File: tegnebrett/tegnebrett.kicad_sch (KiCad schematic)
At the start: 45 parts, among them J1 FH12-45S-0.5SH55, J2 FH12-6S-1SH55, J3 Conn_ST_STDC14, J4 USB-A1HSW6, J5 MCU_Header_Pin, SW1 SW_Push, SW2 SW_Push, SW3 MCU_Button, SW4 Reset, SW5 Undo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

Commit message: fix: fix footprint paths for symbols
After moving the footprints around, some symbols were without
footprints.
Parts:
- J4: footprint USB-A1HSW6:OST_USB-A1HSW6 -> tegnebrett_modules:OST_USB-A1HSW6
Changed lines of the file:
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@@
 			)
 		)
-		(property "Footprint" "USB-A1HSW6:OST_USB-A1HSW6"
+		(property "Footprint" "tegnebrett_modules:OST_USB-A1HSW6"
 			(at 254 73.66 0)
 			(effects

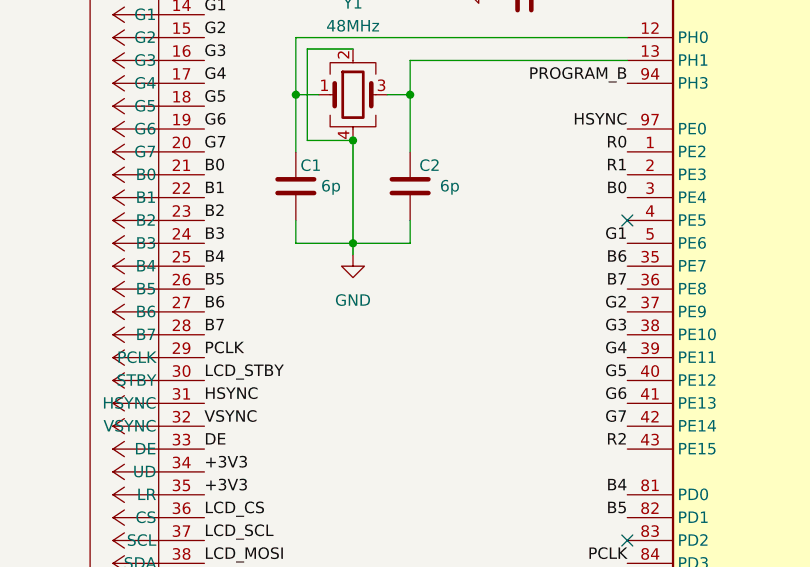
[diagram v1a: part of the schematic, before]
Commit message: fix: Fix error saying that Ground pin isn't powered by power source.
Did this by adding a PWR_FLAG to the schematic.
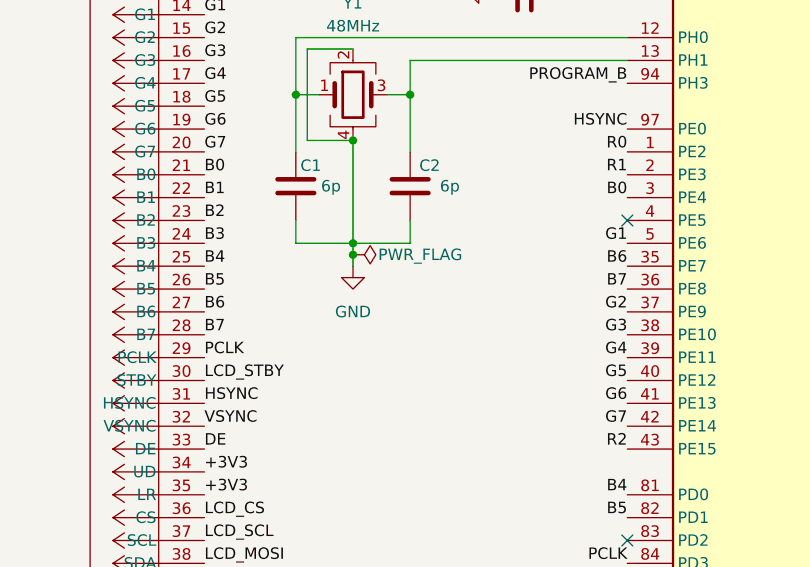
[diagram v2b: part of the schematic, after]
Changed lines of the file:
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@@
 	)
 	(junction
+		(at 53.34 90.17)
+		(diameter 0)
+		(color 0 0 0 0)
+	)
+	(junction
 		(at 231.14 30.48)
 		(diameter 0)
@@
 	(wire
 		(pts
+			(xy 53.34 90.17) (xy 53.34 91.44)
+		)
+		(stroke
+			(width 0)
+			(type default)
+		)
+	)
+	(wire
+		(pts
 			(xy 60.96 156.21) (xy 60.96 168.91)
 		)
@@
 	)
 	(symbol
+		(lib_id "power:PWR_FLAG")
+		(at 53.34 90.17 270)
+		(unit 1)
+		(exclude_from_sim no)
+		(in_bom yes)
+		(on_board yes)
+		(dnp no)
+		(property "Reference" "#FLG08"
+			(at 55.245 90.17 0)
+			(effects
+				(font
+					(size 1.27 1.27)
+				)
+				(hide yes)
+			)
+		)
+		(property "Value" "PWR_FLAG"
+			(at 56.134 90.17 90)
+			(effects
+				(font
+					(size 1.27 1.27)
+				)
+				(justify left)
+			)
+		)
+		(property "Footprint" ""
+			(at 53.34 90.17 0)
+			(effects
+				(font
+					(size 1.27 1.27)
+				)
+				(hide yes)
+			)
+		)
+		(property "Datasheet" "~"
+			(at 53.34 90.17 0)
+			(effects
+				(font
+					(size 1.27 1.27)
+				)
+				(hide yes)
+			)
+		)
+		(property "Description" "Special symbol for telling ERC where power comes from"
+			(at 53.34 90.17 0)
+			(effects
+				(font
+					(size 1.27 1.27)
+				)
+				(hide yes)
+			)
+		)
+		(pin "1"
+		)
+		(instances
+			(project ""
+				(path "/d9a31669-c5f1-42a7-9461-3df04b9a4e62"
+					(reference "#FLG08")
+					(unit 1)
+				)
+			)
+		)
+	)
+	(symbol
 		(lib_id "power:GND")
 		(at 162.56 96.52 90)
@@
 	(symbol
 		(lib_id "power:GND")
-		(at 53.34 90.17 0)
+		(at 53.34 91.44 0)
 		(unit 1)
 		(exclude_from_sim no)
@@
 		(fields_autoplaced yes)
 		(property "Reference" "#PWR01"
-			(at 53.34 96.52 0)
+			(at 53.34 97.79 0)
 			(effects
 				(font
@@
 		)
 		(property "Value" "GND"
-			(at 53.34 95.25 0)
+			(at 53.34 96.52 0)
 			(effects
 				(font
@@
 		)
 		(property "Footprint" ""
-			(at 53.34 90.17 0)
+			(at 53.34 91.44 0)
 			(effects
 				(font
@@
 		)
 		(property "Datasheet" ""
-			(at 53.34 90.17 0)
+			(at 53.34 91.44 0)
 			(effects
 				(font
@@
 		)
 		(property "Description" "Power symbol creates a global label with name \"GND\" , ground"
-			(at 53.34 90.17 0)
+			(at 53.34 91.44 0)
 			(effects
 				(font

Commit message: feat: add FH12 symbols
These were lost somewhere in the process. We're getting KiCAD warnings
because the former library no longer exists.
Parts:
- J1: symbol 2025-09-15_10-55-53:FH12-45S-0.5SH55 -> tegnebrett_symbols:FH12-45S-0.5SH55
- J2: symbol 2025-09-15_09-29-33:FH12-6S-1SH55 -> tegnebrett_symbols:FH12-6S-1SH55
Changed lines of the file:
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@@
 	)
 	(symbol
-		(lib_id "2025-09-15_09-29-33:FH12-6S-1SH55")
+		(lib_id "tegnebrett_symbols:FH12-6S-1SH55")
 		(at 36.83 166.37 180)
 		(unit 1)
@@
 		)
 		(property "Footprint" "tegnebrett_modules:CON6_1X6_DRBF_HST_HIR"
-			(at 36.83 166.37 0)
+			(at 32.512 175.26 0)
 			(effects
 				(font
@@
 		)
 		(property "Datasheet" "FH12-6S-1SH55"
-			(at 36.83 166.37 0)
+			(at 32.258 177.292 0)
 			(effects
 				(font
@@
 		)
 		(property "Sim.Library" "./"
-			(at 36.83 166.37 0)
+			(at 36.83 170.688 0)
 			(effects
 				(font
@@
 		)
 		(property "Sim.Name" "<unbekannt>"
-			(at 36.83 166.37 0)
+			(at 39.37 173.228 0)
 			(effects
 				(font
@@
 	)
 	(symbol
-		(lib_id "2025-09-15_10-55-53:FH12-45S-0.5SH55")
+		(lib_id "tegnebrett_symbols:FH12-45S-0.5SH55")
 		(at 36.83 30.48 0)
 		(mirror y)

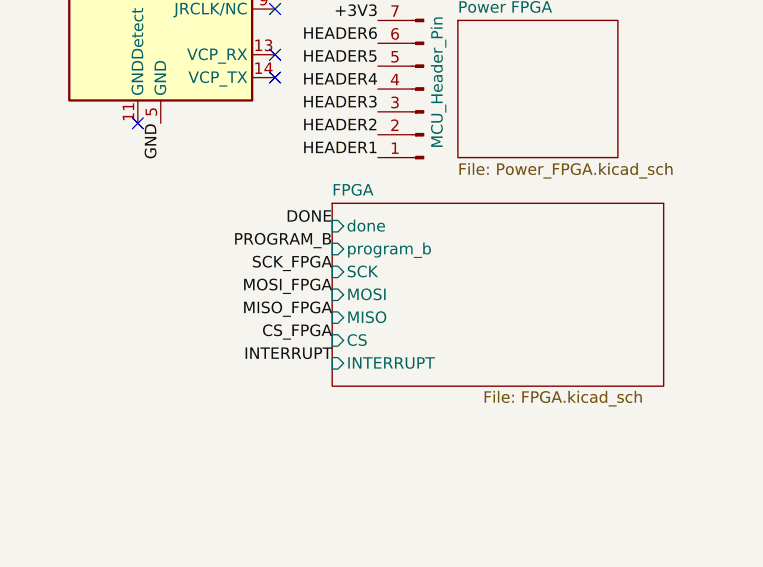
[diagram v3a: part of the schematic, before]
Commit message: refactor: Update label names for hierarchical labels.
Renamed the hierarchical labels in FPGA.kicad_sch, they now are named
the say as the local labels in tegnebrett.kicad_sch

This results in KiCAD no longer throwing any warnings telling us that we
have labels which only differ in casing (upper case / lower case).
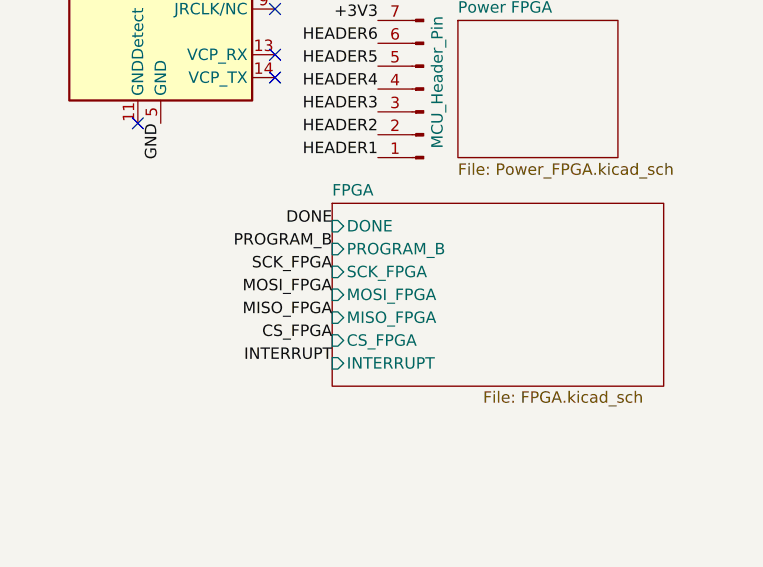
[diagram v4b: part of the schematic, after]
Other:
- sheet FPGA ports: added CS_FPGA, DONE, MISO_FPGA, MOSI_FPGA, PROGRAM_B, SCK_FPGA; removed CS, MISO, MOSI, SCK, done, program_b
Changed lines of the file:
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@@
 	)
 	(label "DONE"
-		(at 246.38 132.08 180)
-		(effects
-			(font
-				(size 1.27 1.27)
-			)
-			(justify right bottom)
-		)
-	)
-	(label "DONE"
 		(at 144.78 109.22 0)
 		(effects
@@
 		)
 	)
+	(label "DONE"
+		(at 246.38 132.08 180)
+		(effects
+			(font
+				(size 1.27 1.27)
+			)
+			(justify right bottom)
+		)
+	)
 	(label "INTERRUPT"
 		(at 246.38 147.32 180)
@@
 			)
 		)
-		(pin "done" input
+		(pin "DONE" input
 			(at 246.38 132.08 180)
 			(effects
@@
 			)
 		)
-		(pin "program_b" input
+		(pin "PROGRAM_B" input
 			(at 246.38 134.62 180)
 			(effects
@@
 			)
 		)
-		(pin "CS" input
+		(pin "CS_FPGA" input
 			(at 246.38 144.78 180)
 			(effects
@@
 			)
 		)
-		(pin "MISO" input
+		(pin "MISO_FPGA" input
 			(at 246.38 142.24 180)
 			(effects
@@
 			)
 		)
-		(pin "MOSI" input
+		(pin "MOSI_FPGA" input
 			(at 246.38 139.7 180)
 			(effects
@@
 			)
 		)
-		(pin "SCK" input
+		(pin "SCK_FPGA" input
 			(at 246.38 137.16 180)
 			(effects

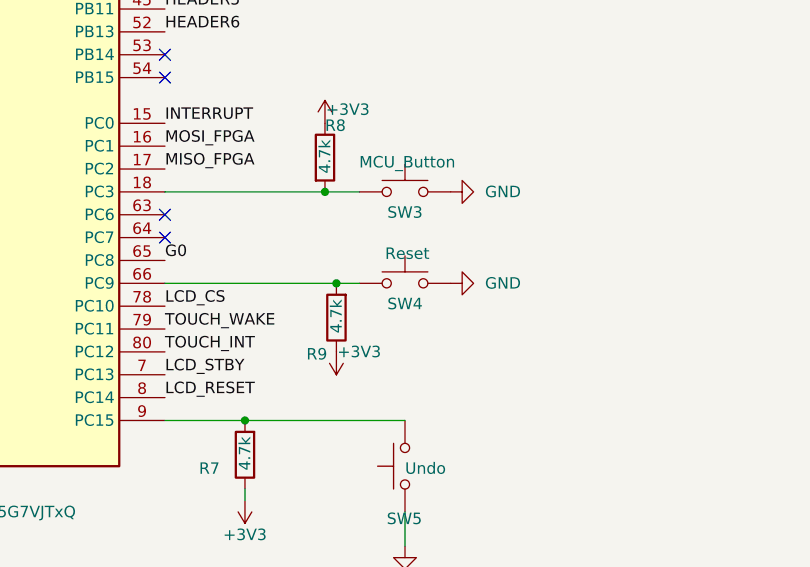
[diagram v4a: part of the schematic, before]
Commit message: fix: add separate symbols for larger switches.
They need pin1 and pin3, not pin1 and pin2.
The PCB editor throws an error when pin3 is not present on the button
symbol.
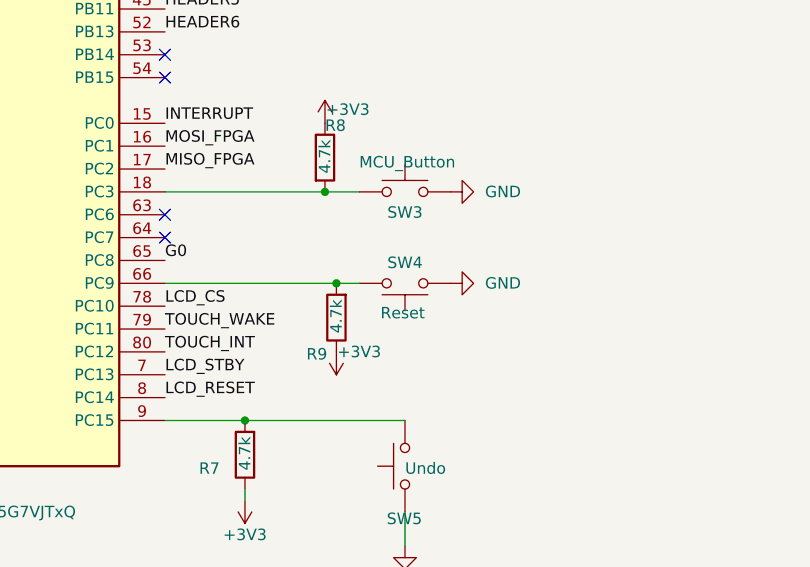
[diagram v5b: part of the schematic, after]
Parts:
- SW4, SW5: symbol Switch:SW_Push -> tegnebrett_symbols:SW_Push_1_3
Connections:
- net GND: now also SW4.1; no longer SW4.2
- net at R9.2, U1.66 (PC9): now also SW4.3; no longer SW4.1
- net at R7.2, U1.9 (PC15): now also SW5.3; no longer SW5.2
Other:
- moved on the sheet: SW4
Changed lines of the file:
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@@
 	)
 	(symbol
-		(lib_id "Switch:SW_Push")
-		(at 171.45 154.94 0)
+		(lib_id "tegnebrett_symbols:SW_Push_1_3")
+		(at 171.45 154.94 180)
 		(unit 1)
 		(exclude_from_sim no)
@@
 		(dnp no)
 		(property "Reference" "SW4"
-			(at 171.45 157.226 0)
+			(at 171.45 152.654 0)
 			(effects
 				(font
@@
 		)
 		(property "Value" "Reset"
-			(at 171.704 151.638 0)
+			(at 171.196 158.242 0)
 			(effects
 				(font
@@
 		)
 		(property "Footprint" "tegnebrett_modules:SW_KS11R23CQD"
-			(at 171.45 149.86 0)
+			(at 171.45 160.02 0)
 			(effects
 				(font
@@
 		)
 		(property "Datasheet" "~"
-			(at 171.45 149.86 0)
+			(at 171.45 160.02 0)
 			(effects
 				(font
@@
 		)
 		(property "Description" "Push button switch, generic, two pins"
-			(at 171.45 154.94 0)
-			(effects
-				(font
-					(size 1.27 1.27)
-				)
-				(hide yes)
-			)
-		)
-		(pin "1"
-		)
-		(pin "2"
+			(at 171.45 150.368 0)
+			(effects
+				(font
+					(size 1.27 1.27)
+				)
+				(hide yes)
+			)
+		)
+		(pin "1"
+		)
+		(pin "3"
 		)
 		(instances
@@
 	)
 	(symbol
-		(lib_id "Switch:SW_Push")
+		(lib_id "tegnebrett_symbols:SW_Push_1_3")
 		(at 171.45 175.26 90)
 		(unit 1)
@@
 		)
 		(property "Description" "Push button switch, generic, two pins"
-			(at 171.45 175.26 0)
-			(effects
-				(font
-					(size 1.27 1.27)
-				)
-				(hide yes)
-			)
-		)
-		(pin "1"
-		)
-		(pin "2"
-		)
-		(instances
+			(at 176.022 175.26 0)
+			(effects
+				(font
+					(size 1.27 1.27)
+				)
+				(hide yes)
+			)
+		)
+		(pin "1"
+		)
+		(pin "3"
+		)
+		(instances

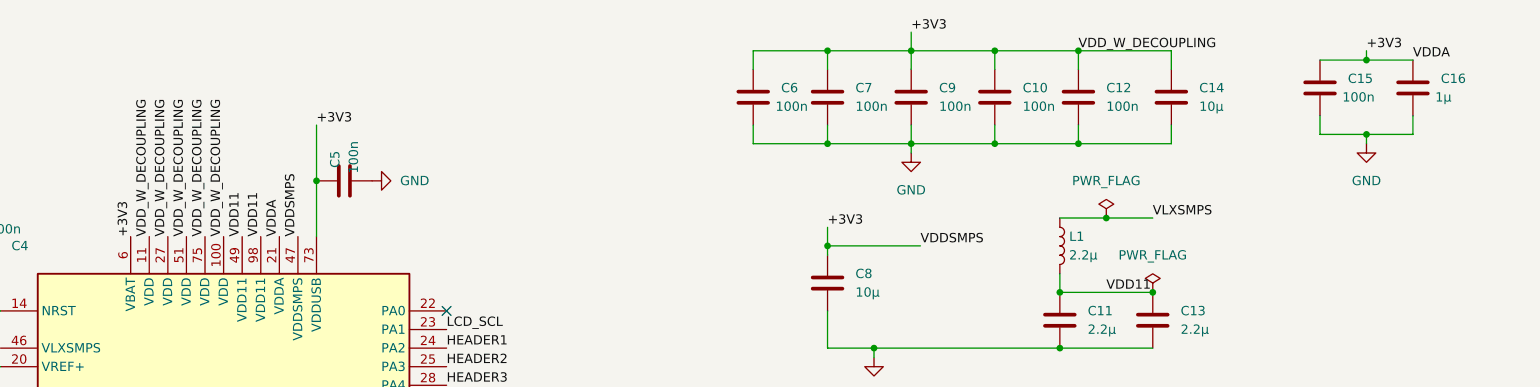
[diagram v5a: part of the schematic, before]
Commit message: fix: remove unused net labels in main MCU sheet
I had used labels called *VDD_W_DECOUPLING* and so forth, but these were
identical in nature to +3V3. The chatbot is saying that we ideally
should have different subnets (whatever that means). Would be necessary
in larger projects, but it's fine to have just +3V3 in this small
schematic/PCB layout.

This removed the last warning in the ERC checker for the schematic.
We're now at 0 errors and 0 warnings there.
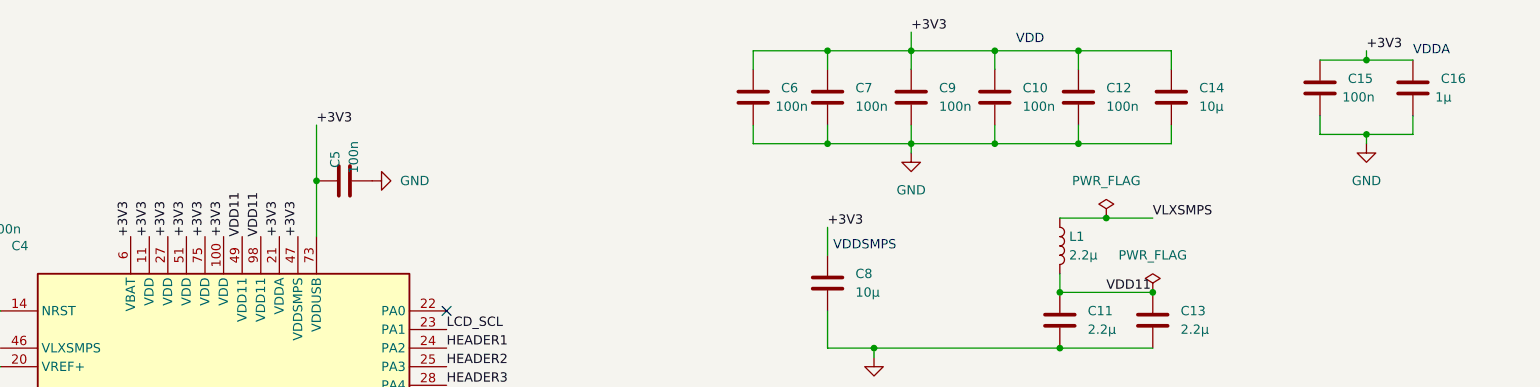
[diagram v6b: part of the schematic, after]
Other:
- note added: "VDD"
- note added: "VDDA"
- note added: "VDDSMPS"
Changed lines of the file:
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@@
 	(generator_version "9.0")
 	(paper "A4")
+	(text "VDD"
+		(exclude_from_sim no)
+		(at 224.536 16.256 0)
+		(effects
+			(font
+				(size 1.27 1.27)
+			)
+		)
+	)
+	(text "VDDSMPS"
+		(exclude_from_sim no)
+		(at 201.93 44.45 0)
+		(effects
+			(font
+				(size 1.27 1.27)
+			)
+		)
+	)
+	(text "VDDA"
+		(exclude_from_sim no)
+		(at 279.4 17.78 0)
+		(effects
+			(font
+				(size 1.27 1.27)
+			)
+		)
+	)
 	(junction
 		(at 228.6 50.8)
@@
 	(junction
 		(at 231.14 30.48)
-		(diameter 0)
-		(color 0 0 0 0)
-	)
-	(junction
-		(at 196.85 44.45)
 		(diameter 0)
 		(color 0 0 0 0)
@@
 	(wire
 		(pts
-			(xy 196.85 41.91) (xy 196.85 44.45)
-		)
-		(stroke
-			(width 0)
-			(type default)
-		)
-	)
-	(wire
-		(pts
 			(xy 240.03 76.2) (xy 243.84 76.2)
 		)
@@
 	(wire
 		(pts
-			(xy 196.85 44.45) (xy 209.55 44.45)
-		)
-		(stroke
-			(width 0)
-			(type default)
-		)
-	)
-	(wire
-		(pts
 			(xy 54.61 158.75) (xy 66.04 158.75)
 		)
@@
 	(wire
 		(pts
-			(xy 196.85 44.45) (xy 196.85 45.72)
+			(xy 196.85 41.91) (xy 196.85 45.72)
 		)
 		(stroke
@@
 		)
 	)
-	(label "VDDSMPS"
-		(at 209.55 44.45 0)
-		(effects
-			(font
-				(size 1.27 1.27)
-			)
-			(justify left bottom)
-		)
-	)
 	(label "DEBUG_SWCLK"
 		(at 252.73 95.25 0)
@@
 		)
 	)
+	(label "+3V3"
+		(at 114.3 43.18 90)
+		(effects
+			(font
+				(size 1.27 1.27)
+			)
+			(justify left bottom)
+		)
+	)
 	(label "R2"
 		(at 83.82 111.76 180)
@@
 		)
 	)
-	(label "VDDA"
-		(at 121.92 43.18 90)
-		(effects
-			(font
-				(size 1.27 1.27)
-			)
-			(justify left bottom)
-		)
-	)
 	(label "R5"
 		(at 36.83 53.34 0)
@@
 		)
 	)
-	(label "VDD_W_DECOUPLING"
-		(at 104.14 43.18 90)
-		(effects
-			(font
-				(size 1.27 1.27)
-			)
-			(justify left bottom)
-		)
-	)
 	(label "GND"
 		(at 116.84 180.34 270)
@@
 		)
 	)
-	(label "VDD_W_DECOUPLING"
-		(at 109.22 43.18 90)
-		(effects
-			(font
-				(size 1.27 1.27)
-			)
-			(justify left bottom)
-		)
-	)
 	(label "DE"
 		(at 83.82 132.08 180)
@@
 		)
 	)
+	(label "+3V3"
+		(at 106.68 43.18 90)
+		(effects
+			(font
+				(size 1.27 1.27)
+			)
+			(justify left bottom)
+		)
+	)
 	(label "INTERRUPT"
 		(at 144.78 137.16 0)
@@
 		)
 	)
+	(label "+3V3"
+		(at 111.76 43.18 90)
+		(effects
+			(font
+				(size 1.27 1.27)
+			)
+			(justify left bottom)
+		)
+	)
 	(label "DEBUG_SWDIO"
 		(at 144.78 86.36 0)
@@
 		)
 	)
-	(label "VDD_W_DECOUPLING"
-		(at 231.14 17.78 0)
-		(effects
-			(font
-				(size 1.27 1.27)
-			)
-			(justify left bottom)
-		)
-	)
 	(label "DONE"
 		(at 246.38 132.08 180)
@@
 		)
 	)
-	(label "VDDA"
-		(at 276.86 19.05 0)
-		(effects
-			(font
-				(size 1.27 1.27)
-			)
-			(justify left bottom)
-		)
-	)
 	(label "HEADER1"
 		(at 144.78 58.42 0)
@@
 		)
 	)
-	(label "VDD_W_DECOUPLING"
-		(at 106.68 43.18 90)
-		(effects
-			(font
-				(size 1.27 1.27)
-			)
-			(justify left bottom)
-		)
-	)
 	(label "DEBUG_SWDIO"
 		(at 252.73 97.79 0)
@@
 		)
 	)
+	(label "+3V3"
+		(at 121.92 43.18 90)
+		(effects
+			(font
+				(size 1.27 1.27)
+			)
+			(justify left bottom)
+		)
+	)
 	(label "MOSI_FPGA"
 		(at 144.78 139.7 0)
@@
 		)
 	)
-	(label "VDD_W_DECOUPLING"
-		(at 114.3 43.18 90)
-		(effects
-			(font
-				(size 1.27 1.27)
-			)
-			(justify left bottom)
-		)
-	)
-	(label "VDD_W_DECOUPLING"
-		(at 111.76 43.18 90)
-		(effects
-			(font
-				(size 1.27 1.27)
-			)
-			(justify left bottom)
-		)
-	)
 	(label "+3V3"
 		(at 36.83 35.56 0)
@@
 		)
 	)
-	(label "VDDSMPS"
-		(at 124.46 43.18 90)
-		(effects
-			(font
-				(size 1.27 1.27)
-			)
-			(justify left bottom)
-		)
-	)
 	(label "GND"
 		(at 114.3 180.34 270)
@@
 		)
 	)
+	(label "+3V3"
+		(at 104.14 43.18 90)
+		(effects
+			(font
+				(size 1.27 1.27)
+			)
+			(justify left bottom)
+		)
+	)
 	(label "TOUCH_SCL"
 		(at 66.04 166.37 0)
@@
 		)
 	)
+	(label "+3V3"
+		(at 109.22 43.18 90)
+		(effects
+			(font
+				(size 1.27 1.27)
+			)
+			(justify left bottom)
+		)
+	)
 	(label "LCD_CS"
 		(at 144.78 157.48 0)
@@
 		)
 	)
+	(label "+3V3"
+		(at 124.46 43.18 90)
+		(effects
+			(font
+				(size 1.27 1.27)
+			)
+			(justify left bottom)
+		)
+	)
